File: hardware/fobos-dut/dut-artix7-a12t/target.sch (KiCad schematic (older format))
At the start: 34 parts, among them J1 Target, J2 Pmod 2x6, U2 SP3003-04ATG, U3 SP3003-04ATG, U4 SP3003-04ATG, U7 TS3A27518EIPWRQ1

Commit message: Schematic is 99% complete, getting started on layout
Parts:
- J2: footprint (none) -> Connector_PinHeader_2.54mm:PinHeader_2x06_P2.54mm_Horizontal
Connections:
- net labels added: +3V3
- net labels removed: VCCIO
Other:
- note added: "Make footprint compatible with Digilent inc PMOD standard"
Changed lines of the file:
@@
 $Descr USLetter 11000 8500
 encoding utf-8
-Sheet 2 6
+Sheet 2 7
 Title "FOBOS Artix-7 a12t DUT - Connectors, IO"
 Date "2020-07-28"
@@
 F 0 "J2" H 8250 6067 50  0000 C CNN
 F 1 "Pmod 2x6" H 8250 5976 50  0000 C CNN
-F 2 "" H 8200 5650 50  0001 C CNN
+F 2 "Connector_PinHeader_2.54mm:PinHeader_2x06_P2.54mm_Horizontal" H 8200 5650 50  0001 C CNN
 F 3 "~" H 8200 5650 50  0001 C CNN
 	1    8200 5650
@@
 	7850 5850 7850 6050
 Wire Wire Line
-	8250 6350 8250 6250
-Wire Wire Line
 	8250 6350 8550 6350
 Wire Wire Line
@@
 Wire Wire Line
 	4000 2500 4250 2500
-$Comp
-L cerg:VCCIO #PWR0111
-U 1 1 5F26D720
-P 8250 6250
-F 0 "#PWR0111" H 8250 6100 50  0001 C CNN
-F 1 "VCCIO" V 8150 6350 50  0000 C CNN
-F 2 "" H 8250 6250 50  0001 C CNN
-F 3 "" H 8250 6250 50  0001 C CNN
-	1    8250 6250
-	1    0    0    -1
-$EndComp
 Text GLabel 9900 3700 2    50   Input ~ 0
 (Aux)FC_PROG
@@
 	1    0    0    -1
 $EndComp
+Text Notes 7100 6500 0    50   ~ 0
+Make footprint compatible with Digilent inc PMOD standard
+$Comp
+L power:+3V3 #PWR?
+U 1 1 60336087
+P 8250 6300
+AR Path="/5F3A1954/60336087" Ref="#PWR?"  Part="1"
+AR Path="/5F20DA36/60336087" Ref="#PWR0111"  Part="1"
+F 0 "#PWR0111" H 8250 6150 50  0001 C CNN
+F 1 "+3V3" H 8265 6473 50  0000 C CNN
+F 2 "" H 8250 6300 50  0001 C CNN
+F 3 "" H 8250 6300 50  0001 C CNN
+	1    8250 6300
+	1    0    0    -1
+$EndComp
+Wire Wire Line
+	8250 6300 8250 6350
 $EndSCHEMATC

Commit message: Preliminary placement underway Made a copy of cerg 3d model within Artix 7 dut project to resolve nagging library path issue
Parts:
- removed U7: TS3A27518EIPWRQ1, Package_SO:TSSOP-24_4.4x7.8mm_P0.65mm, symbol cerg:TS3A27518EIPWRQ1
- added R67: 0R, Resistor_SMD:R_0603_1608Metric, symbol Device:R
- added U7: TS3A5018DBQR, cerg:SSOP-16_4.0x5.0mm_P0.635mm, symbol cerg:TS3A5018DBQR
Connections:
- wire segments 169 -> 167
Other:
- moved on the sheet: C54, R51
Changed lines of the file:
@@
 	1    0    0    1
 $EndComp
-Text GLabel 1550 5050 0    50   Input ~ 0
+Text GLabel 1750 5250 0    50   Input ~ 0
 FC_PROG
-Text GLabel 2700 5550 0    50   Input ~ 0
-FD_TF
-Text GLabel 2700 5350 0    50   Input ~ 0
-SW_DONE
 Text Notes 2200 4050 0    79   ~ 0
 Programming/DUT Communication Switches
@@
 L Device:R R?
 U 1 1 60131BF4
-P 1850 5250
+P 2050 5450
 AR Path="/5F227C5D/60131BF4" Ref="R?"  Part="1"
 AR Path="/5F20DA36/60131BF4" Ref="R51"  Part="1"
-F 0 "R51" V 1750 5200 50  0000 L CNN
-F 1 "10KR" V 1950 5150 50  0000 L CNN
-F 2 "Resistor_SMD:R_0603_1608Metric" V 1780 5250 50  0001 C CNN
-F 3 "~" H 1850 5250 50  0001 C CNN
-	1    1850 5250
+F 0 "R51" V 1950 5400 50  0000 L CNN
+F 1 "10KR" V 2150 5350 50  0000 L CNN
+F 2 "Resistor_SMD:R_0603_1608Metric" V 1980 5450 50  0001 C CNN
+F 3 "~" H 2050 5450 50  0001 C CNN
+	1    2050 5450
 	-1   0    0    1
 $EndComp
 Wire Wire Line
-	1850 5100 1850 5050
-$Comp
-L cerg:TS3A27518EIPWRQ1 U7
-U 1 1 601820C1
-P 3000 4950
-F 0 "U7" H 3650 5000 50  0000 C CNN
-F 1 "TS3A27518EIPWRQ1" H 4000 3400 50  0000 C CNN
-F 2 "Package_SO:TSSOP-24_4.4x7.8mm_P0.65mm" H 4000 5200 50  0001 C CNN
-F 3 "https://www.digikey.com/en/products/detail/texas-instruments/TS3A27518EIPWRQ1/2520836" H 4000 5200 50  0001 C CNN
-	1    3000 4950
-	1    0    0    -1
-$EndComp
-Text GLabel 2700 5850 0    50   Input ~ 0
-FC_DIO0_MUX
-Text GLabel 2700 5750 0    50   Input ~ 0
-SW_CLK
-Text GLabel 2700 5950 0    50   Input ~ 0
-FC_DIO0
-Text GLabel 2700 6300 0    50   Input ~ 0
-FC_DIO1
-Text GLabel 2700 6200 0    50   Input ~ 0
-FC_DIO1_MUX
-Text GLabel 2700 6100 0    50   Input ~ 0
-SW_DIN
-Text GLabel 4250 5550 2    50   Input ~ 0
-FC_DIO2
-Text GLabel 4250 5350 2    50   Input ~ 0
-SW_PROGRAM_B
-Text GLabel 4250 5450 2    50   Input ~ 0
-FC_DIO2_MUX
-Text GLabel 4250 5850 2    50   Input ~ 0
-FC_DIO3_MUX
-Text GLabel 4250 5750 2    50   Input ~ 0
-SW_INIT_B
-Text GLabel 4250 5950 2    50   Input ~ 0
-FC_DIO3
-Wire Wire Line
-	2700 5350 2900 5350
-Wire Wire Line
-	2700 5550 2900 5550
-Wire Wire Line
-	2700 5750 2900 5750
-Wire Wire Line
-	2700 5850 2900 5850
-Wire Wire Line
-	2700 5950 2900 5950
-Wire Wire Line
-	2700 6100 2900 6100
-Wire Wire Line
-	2700 6200 2900 6200
-Wire Wire Line
-	2700 6300 2900 6300
-Wire Wire Line
-	4250 5350 4050 5350
-Wire Wire Line
-	4250 5450 4050 5450
-Wire Wire Line
-	4250 5550 4050 5550
-Wire Wire Line
-	4250 5750 4050 5750
-Wire Wire Line
-	4250 5850 4050 5850
-Wire Wire Line
-	4250 5950 4050 5950
+	2050 5300 2050 5250
 $Comp
 L Device:C C?
 U 1 1 6025643D
-P 4350 4700
+P 4850 5500
 AR Path="/5F227C5D/6025643D" Ref="C?"  Part="1"
 AR Path="/5F20DA36/6025643D" Ref="C54"  Part="1"
-F 0 "C54" V 4200 4650 50  0000 L CNN
-F 1 "100nF" V 4500 4550 50  0000 L CNN
-F 2 "Capacitor_SMD:C_0603_1608Metric" H 4388 4550 50  0001 C CNN
-F 3 "~" H 4350 4700 50  0001 C CNN
-	1    4350 4700
-	1    0    0    -1
-$EndComp
-Text GLabel 4500 4450 2    50   Input ~ 0
+F 0 "C54" V 4700 5450 50  0000 L CNN
+F 1 "100nF" V 5000 5350 50  0000 L CNN
+F 2 "Capacitor_SMD:C_0603_1608Metric" H 4888 5350 50  0001 C CNN
+F 3 "~" H 4850 5500 50  0001 C CNN
+	1    4850 5500
+	1    0    0    -1
+$EndComp
+Text GLabel 5000 5250 2    50   Input ~ 0
 FC_3V3
 Wire Wire Line
-	3450 4850 3450 4450
-Wire Wire Line
-	3450 4450 4150 4450
-Wire Wire Line
-	4350 4550 4350 4450
-Connection ~ 4350 4450
-Wire Wire Line
-	4350 4450 4500 4450
-Wire Wire Line
-	4050 5050 4150 5050
-Wire Wire Line
-	4150 5050 4150 4450
-Connection ~ 4150 4450
-Wire Wire Line
-	4150 4450 4350 4450
+	4850 5350 4850 5250
+Connection ~ 4850 5250
+Wire Wire Line
+	4850 5250 5000 5250
 $Comp
 L power:GND #PWR?
 U 1 1 602946AE
-P 4350 4850
+P 4850 5650
 AR Path="/5B6C87CC/602946AE" Ref="#PWR?"  Part="1"
 AR Path="/5B5AB131/602946AE" Ref="#PWR?"  Part="1"
@@
 AR Path="/5F227C5D/602946AE" Ref="#PWR?"  Part="1"
 AR Path="/5F20DA36/602946AE" Ref="#PWR041"  Part="1"
-F 0 "#PWR041" H 4350 4600 50  0001 C CNN
-F 1 "GND" H 4355 4677 50  0000 C CNN
-F 2 "" H 4350 4850 50  0001 C CNN
-F 3 "" H 4350 4850 50  0001 C CNN
-	1    4350 4850
-	1    0    0    -1
-$EndComp
-Wire Wire Line
-	1550 5050 1850 5050
-Wire Wire Line
-	2900 5050 2800 5050
-Connection ~ 1850 5050
+F 0 "#PWR041" H 4850 5400 50  0001 C CNN
+F 1 "GND" H 4855 5477 50  0000 C CNN
+F 2 "" H 4850 5650 50  0001 C CNN
+F 3 "" H 4850 5650 50  0001 C CNN
+	1    4850 5650
+	1    0    0    -1
+$EndComp
+Wire Wire Line
+	1750 5250 2050 5250
 $Comp
 L power:GND #PWR?
 U 1 1 602A9678
-P 1850 5400
+P 2050 5600
 AR Path="/5B6C87CC/602A9678" Ref="#PWR?"  Part="1"
 AR Path="/5B5AB131/602A9678" Ref="#PWR?"  Part="1"
@@
 AR Path="/5F227C5D/602A9678" Ref="#PWR?"  Part="1"
 AR Path="/5F20DA36/602A9678" Ref="#PWR039"  Part="1"
-F 0 "#PWR039" H 1850 5150 50  0001 C CNN
-F 1 "GND" H 1855 5227 50  0000 C CNN
-F 2 "" H 1850 5400 50  0001 C CNN
-F 3 "" H 1850 5400 50  0001 C CNN
-	1    1850 5400
-	1    0    0    -1
-$EndComp
-Wire Wire Line
-	2900 5150 2800 5150
-Wire Wire Line
-	2800 5150 2800 5050
-Connection ~ 2800 5050
-Wire Wire Line
-	2800 5050 1850 5050
-$Comp
-L power:GND #PWR?
-U 1 1 602B3FF7
-P 3450 6500
-AR Path="/5B6C87CC/602B3FF7" Ref="#PWR?"  Part="1"
-AR Path="/5B5AB131/602B3FF7" Ref="#PWR?"  Part="1"
-AR Path="/5BE3725D/602B3FF7" Ref="#PWR?"  Part="1"
-AR Path="/5F227C5D/602B3FF7" Ref="#PWR?"  Part="1"
-AR Path="/5F20DA36/602B3FF7" Ref="#PWR040"  Part="1"
-F 0 "#PWR040" H 3450 6250 50  0001 C CNN
-F 1 "GND" H 3455 6327 50  0000 C CNN
-F 2 "" H 3450 6500 50  0001 C CNN
-F 3 "" H 3450 6500 50  0001 C CNN
-	1    3450 6500
+F 0 "#PWR039" H 2050 5350 50  0001 C CNN
+F 1 "GND" H 2055 5427 50  0000 C CNN
+F 2 "" H 2050 5600 50  0001 C CNN
+F 3 "" H 2050 5600 50  0001 C CNN
+	1    2050 5600
 	1    0    0    -1
 $EndComp
@@
 Wire Wire Line
 	8250 6300 8250 6350
+$Comp
+L cerg:TS3A5018DBQR U7
+U 1 1 602ABBA0
+P 3100 5150
+F 0 "U7" H 3425 5315 50  0000 C CNN
+F 1 "TS3A5018DBQR" H 3425 5224 50  0000 C CNN
+F 2 "cerg:SSOP-16_4.0x5.0mm_P0.635mm" H 3000 5400 50  0001 C CNN
+F 3 "https://www.digikey.com/en/products/detail/texas-instruments/TS3A5018DBQR/705733" H 3000 5400 50  0001 C CNN
+	1    3100 5150
+	1    0    0    -1
+$EndComp
+Text GLabel 2900 5450 0    50   Input ~ 0
+SW_CLK
+Text GLabel 2900 5350 0    50   Input ~ 0
+FC_DIO0_MUX
+Text GLabel 2900 5550 0    50   Input ~ 0
+FC_DIO0
+Text GLabel 2900 5750 0    50   Input ~ 0
+SW_DIN
+Text GLabel 2900 5650 0    50   Input ~ 0
+FC_DIO1_MUX
+Text GLabel 2900 5850 0    50   Input ~ 0
+FC_DIO1
+Text GLabel 4000 5950 2    50   Input ~ 0
+FC_DIO3
+Text GLabel 4000 5750 2    50   Input ~ 0
+FC_DIO3_MUX
+Text GLabel 4000 5850 2    50   Input ~ 0
+SW_INIT_B
+Text GLabel 4000 5650 2    50   Input ~ 0
+FC_DIO2
+Text GLabel 4000 5450 2    50   Input ~ 0
+FC_DIO2_MUX
+Text GLabel 4000 5550 2    50   Input ~ 0
+SW_PROGRAM_B
+Wire Wire Line
+	3000 5250 2050 5250
+Connection ~ 2050 5250
+Wire Wire Line
+	3000 5350 2900 5350
+Wire Wire Line
+	3000 5450 2900 5450
+Wire Wire Line
+	3000 5550 2900 5550
+Wire Wire Line
+	3000 5650 2900 5650
+Wire Wire Line
+	3000 5750 2900 5750
+Wire Wire Line
+	3000 5850 2900 5850
+Wire Wire Line
+	4000 5450 3850 5450
+Wire Wire Line
+	4000 5550 3850 5550
+Wire Wire Line
+	4000 5650 3850 5650
+Wire Wire Line
+	4000 5750 3850 5750
+Wire Wire Line
+	4000 5850 3850 5850
+Wire Wire Line
+	4000 5950 3850 5950
+Wire Wire Line
+	3850 5250 4000 5250
+Wire Wire Line
+	3850 5350 4000 5350
+Wire Wire Line
+	4000 5350 4000 5250
+Connection ~ 4000 5250
+Wire Wire Line
+	4000 5250 4850 5250
+Text GLabel 2650 6500 0    50   Input ~ 0
+SW_DONE
+Text GLabel 2650 6900 0    50   Input ~ 0
+FD_TF
+$Comp
+L Device:R R?
+U 1 1 603A6505
+P 2850 6700
+AR Path="/5F227C5D/603A6505" Ref="R?"  Part="1"
+AR Path="/5F20DA36/603A6505" Ref="R67"  Part="1"
+F 0 "R67" V 2750 6650 50  0000 L CNN
+F 1 "0R" V 2950 6600 50  0000 L CNN
+F 2 "Resistor_SMD:R_0603_1608Metric" V 2780 6700 50  0001 C CNN
+F 3 "~" H 2850 6700 50  0001 C CNN
+	1    2850 6700
+	-1   0    0    1
+$EndComp
+Wire Wire Line
+	2850 6550 2850 6500
+Wire Wire Line
+	2850 6500 2650 6500
+Wire Wire Line
+	2850 6850 2850 6900
+Wire Wire Line
+	2850 6900 2650 6900
 $EndSCHEMATC

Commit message: Coarse placement of all components within board outline, began to route traces
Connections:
- net labels removed: (Aux)FC_PROG, (Ready)FC2D_HS, (Valid)FD2C_HS
- wire segments 167 -> 169
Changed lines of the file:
@@
 	1    0    0    1
 $EndComp
-Text GLabel 9900 2150 2    50   Input ~ 0
+Text GLabel 8600 1950 0    50   Input ~ 0
 FC_DIO0
 Text GLabel 9900 1950 2    50   Input ~ 0
@@
 	9750 2150 9800 2150
 Wire Wire Line
-	8600 2150 8700 2150
-Text GLabel 8600 1950 0    50   Input ~ 0
+	8600 3700 8700 3700
+Text GLabel 9900 3700 2    50   Input ~ 0
 FC_IO
 Connection ~ 8700 1950
@@
 Wire Wire Line
 	8700 2350 8700 2150
-Connection ~ 8700 2150
 Wire Wire Line
 	8700 2150 8750 2150
@@
 Wire Wire Line
 	9250 2750 9250 2650
-Text GLabel 8600 3700 0    50   Input ~ 0
+Text GLabel 9900 3900 2    50   Input ~ 0
 FC2D_CLK
 Wire Wire Line
-	8600 3700 8700 3700
-Wire Wire Line
 	8600 3900 8700 3900
 Wire Wire Line
@@
 Wire Wire Line
 	8700 3500 8750 3500
-Connection ~ 8700 3700
 Wire Wire Line
 	8700 3700 8750 3700
@@
 Wire Wire Line
 	4000 2500 4250 2500
-Text GLabel 9900 3700 2    50   Input ~ 0
-(Aux)FC_PROG
-Text GLabel 9900 3900 2    50   Input ~ 0
+Text GLabel 7500 2150 2    50   Input ~ 0
+FC_PROG
+Text GLabel 8600 2150 0    50   Input ~ 0
 FD_TF
 Text GLabel 8600 3900 0    50   Input ~ 0
 FD2C_CLK
+Text GLabel 9900 2150 2    50   Input ~ 0
+FC2D_HS
 Text GLabel 6200 2150 0    50   Input ~ 0
-(Ready)FC2D_HS
-Text GLabel 7500 2150 2    50   Input ~ 0
-(Valid)FD2C_HS
+FD2C_HS
 Wire Wire Line
 	7200 1300 7250 1300
@@
 Wire Wire Line
 	6750 1300 6850 1300
-Text GLabel 8600 2150 0    50   Input ~ 0
+Text GLabel 8600 3700 0    50   Input ~ 0
 FC_RST
 Text Notes 7650 1100 0    79   ~ 0
@@
 Wire Wire Line
 	2850 6900 2650 6900
+Connection ~ 8700 3700
+Wire Wire Line
+	8600 2150 8700 2150
+Connection ~ 8700 2150
+$Comp
+L power:GND #PWR?
+U 1 1 60694C99
+P 2850 6100
+AR Path="/5F227C5D/60694C99" Ref="#PWR?"  Part="1"
+AR Path="/5F20DA36/60694C99" Ref="#PWR?"  Part="1"
+F 0 "#PWR?" H 2850 5850 50  0001 C CNN
+F 1 "GND" H 2855 5927 50  0000 C CNN
+F 2 "" H 2850 6100 50  0001 C CNN
+F 3 "" H 2850 6100 50  0001 C CNN
+	1    2850 6100
+	1    0    0    -1
+$EndComp
+Wire Wire Line
+	3000 5950 2850 5950
+Wire Wire Line
+	2850 5950 2850 6100
 $EndSCHEMATC

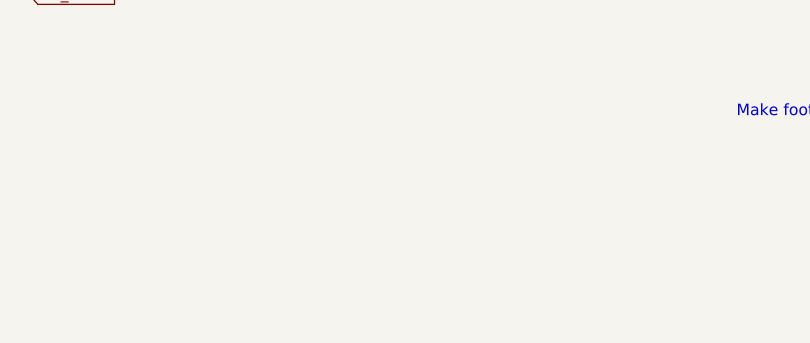
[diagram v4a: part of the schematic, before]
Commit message: Expanded copper pours on layer 3 Connected NC mux pins to the FPGA
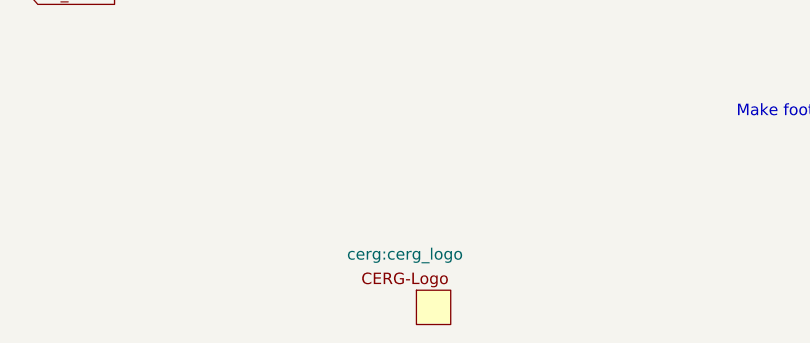
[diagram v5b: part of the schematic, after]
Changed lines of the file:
@@
 Wire Wire Line
 	2850 5950 2850 6100
+$Comp
+L cerg:CERG-logo #LOGO2
+U 1 1 606D810A
+P 5650 7250
+F 0 "#LOGO2" H 5650 7525 50  0001 C CNN
+F 1 "CERG-logo" H 5650 7025 50  0001 C CNN
+F 2 "cerg:cerg_logo" H 5650 7407 50  0000 C CNN
+F 3 "" H 5650 7525 50  0001 C CNN
+	1    5650 7250
+	1    0    0    -1
+$EndComp
 $EndSCHEMATC

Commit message: Added external 5V connector Added shunt for FC3v3 and 3V3 Added silkscreen which clarifies switch functionality Thickened 5 mil traces to 7 mil where feasible Moved Vcore amplifier closer to Vcore pad to reduce amplification of noise
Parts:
- added J10: Conn_01x02, Connector_Molex:Molex_KK-254_AE-6410-02A_1x02_P2.54mm_Vertical, symbol Connector_Generic:Conn_01x02
- added JP4: FC3V3_3V3_SHUNT, Connector_PinHeader_2.54mm:PinHeader_1x02_P2.54mm_Vertical, symbol Jumper:Jumper_2_Open
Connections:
- net labels added: +3.3V
- wire segments 169 -> 174
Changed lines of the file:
@@
 	1    0    0    1
 $EndComp
-Text GLabel 8600 1950 0    50   Input ~ 0
-FC_DIO0
-Text GLabel 9900 1950 2    50   Input ~ 0
-FC_DIO1
-Wire Wire Line
-	8600 1950 8700 1950
 Wire Wire Line
 	9750 1950 9800 1950
@@
 Text GLabel 9900 3700 2    50   Input ~ 0
 FC_IO
-Connection ~ 8700 1950
 Wire Wire Line
 	8700 1950 8750 1950
@@
 Text GLabel 7500 2150 2    50   Input ~ 0
 FC_PROG
-Text GLabel 8600 2150 0    50   Input ~ 0
-FD_TF
 Text GLabel 8600 3900 0    50   Input ~ 0
 FD2C_CLK
-Text GLabel 9900 2150 2    50   Input ~ 0
-FC2D_HS
 Text GLabel 6200 2150 0    50   Input ~ 0
 FD2C_HS
@@
 Text GLabel 1750 5250 0    50   Input ~ 0
 FC_PROG
-Text Notes 2200 4050 0    79   ~ 0
+Text Notes 2250 4900 0    79   ~ 0
 Programming/DUT Communication Switches
 $Comp
@@
 	2850 6900 2650 6900
 Connection ~ 8700 3700
-Wire Wire Line
-	8600 2150 8700 2150
-Connection ~ 8700 2150
 $Comp
 L power:GND #PWR?
@@
 	1    0    0    -1
 $EndComp
+Text GLabel 8600 1950 0    50   Input ~ 0
+FD_TF
+Wire Wire Line
+	8600 1950 8700 1950
+Text GLabel 8600 2150 0    50   Input ~ 0
+FC_DIO0
+Wire Wire Line
+	8600 2150 8700 2150
+Text GLabel 9900 2150 2    50   Input ~ 0
+FC_DIO1
+Text GLabel 9900 1950 2    50   Input ~ 0
+FC2D_HS
+$Comp
+L Connector_Generic:Conn_01x02 J?
+U 1 1 60A59B2F
+P 4300 2850
+AR Path="/5F449901/60A59B2F" Ref="J?"  Part="1"
+AR Path="/5F20DA36/60A59B2F" Ref="J10"  Part="1"
+F 0 "J10" H 4380 2842 50  0000 L CNN
+F 1 "Conn_01x02" H 4380 2751 50  0000 L CNN
+F 2 "Connector_Molex:Molex_KK-254_AE-6410-02A_1x02_P2.54mm_Vertical" H 4300 2850 50  0001 C CNN
+F 3 "~" H 4300 2850 50  0001 C CNN
+	1    4300 2850
+	1    0    0    -1
+$EndComp
+$Comp
+L Jumper:Jumper_2_Open JP?
+U 1 1 60A66495
+P 4200 3350
+AR Path="/5F449901/60A66495" Ref="JP?"  Part="1"
+AR Path="/5F20DA36/60A66495" Ref="JP4"  Part="1"
+F 0 "JP4" H 4200 3585 50  0000 C CNN
+F 1 "FC3V3_3V3_SHUNT" H 4200 3494 50  0000 C CNN
+F 2 "Connector_PinHeader_2.54mm:PinHeader_1x02_P2.54mm_Vertical" H 4200 3350 50  0001 C CNN
+F 3 "~" H 4200 3350 50  0001 C CNN
+	1    4200 3350
+	1    0    0    -1
+$EndComp
+Text GLabel 3800 3350 0    50   Input ~ 0
+FC_3V3
+Text GLabel 3800 2850 0    50   Input ~ 0
+FC_5V
+$Comp
+L power:GND #PWR?
+U 1 1 60A8FBF0
+P 3650 3000
+AR Path="/5B6C87CC/60A8FBF0" Ref="#PWR?"  Part="1"
+AR Path="/5B5AB131/60A8FBF0" Ref="#PWR?"  Part="1"
+AR Path="/5BE3725D/60A8FBF0" Ref="#PWR?"  Part="1"
+AR Path="/5F227C5D/60A8FBF0" Ref="#PWR?"  Part="1"
+AR Path="/5F20DA36/60A8FBF0" Ref="#PWR030"  Part="1"
+F 0 "#PWR030" H 3650 2750 50  0001 C CNN
+F 1 "GND" H 3655 2827 50  0000 C CNN
+F 2 "" H 3650 3000 50  0001 C CNN
+F 3 "" H 3650 3000 50  0001 C CNN
+	1    3650 3000
+	1    0    0    -1
+$EndComp
+Wire Wire Line
+	3800 2850 4100 2850
+Wire Wire Line
+	3650 3000 3650 2950
+Wire Wire Line
+	3650 2950 4100 2950
+Wire Wire Line
+	4000 3350 3800 3350
+$Comp
+L power:+3.3V #PWR?
+U 1 1 60ABDA54
+P 4700 3350
+AR Path="/5F449901/60ABDA54" Ref="#PWR?"  Part="1"
+AR Path="/5F20DA36/60ABDA54" Ref="#PWR031"  Part="1"
+F 0 "#PWR031" H 4700 3200 50  0001 C CNN
+F 1 "+3.3V" H 4715 3523 50  0000 C CNN
+F 2 "" H 4700 3350 50  0001 C CNN
+F 3 "" H 4700 3350 50  0001 C CNN
+	1    4700 3350
+	1    0    0    -1
+$EndComp
+Wire Wire Line
+	4700 3350 4400 3350
 $EndSCHEMATC

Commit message: Added Manufacturer Part Number, Manufacturer to all components except ferrite beads Added digikey quote
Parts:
- C1, C2, C3, C54: Description (none) -> CAP CER 0.1UF 6.3V X7R 0603; MPN (none) -> 06036C104KAT4A; Manufacturer (none) -> AVX Corporation
- J1: Description (none) -> CONN HEADER R/A 20POS 2.54MM; MPN (none) -> 61202021721; Manufacturer (none) -> Würth Elektronik
- J10: Description (none) -> CONN HEADER VERT 2POS 2.54MM; MPN (none) -> 0022272021; Manufacturer (none) -> Molex
- J2: Description (none) -> CONN HEADER R/A 12POS 2.54MM; MPN (none) -> PH2RA-12-UA; Manufacturer (none) -> Adam Tech
- JP4: Description (none) -> CONN HEADER VERT 2POS 2.54MM; MPN (none) -> 10129378-902001BLF; Manufacturer (none) -> Amphenol ICC (FCI)
- R1, R13, R14, R15, R16, R17, R18, R2, R3, R4, R5, R6: Description (none) -> RES 22 OHM 5% 1/10W 0603 SMD; MPN (none) -> ERJ-U03J220V; Manufacturer (none) -> Panasonic Electronic Components
- R10, R11, R12, R19, R20, R7, R8, R9: Description (none) -> RES SMD 200 OHM 0.5% 1/10W 0603; MPN (none) -> ERA-3AED201V; Manufacturer (none) -> Panasonic Electronic Components
- R51: Description (none) -> RES SMD 10K OHM 1% 1/10W 0603; MPN (none) -> ERJ-3EKF1002V; Manufacturer (none) -> Panasonic Electronic Components
- R67: Description (none) -> RES 0 OHM JUMPER 1/10W 0603; MPN (none) -> RMCF0603ZT0R00; Manufacturer (none) -> Stackpole Electronics Inc
- TP2, TP3, TP4: Description (none) -> TEST POINT (BLACK) - MULTIPURPOS; MPN (none) -> 5281; Manufacturer (none) -> Keystone Electronics
- U2, U3, U4: Description (none) -> TVS DIODE 6V 15V 10MSOP; MPN (none) -> SP3003-04ATG; Manufacturer (none) -> Littelfuse Inc.
- U7: Description (none) -> IC SWITCH QUAD SPDT 16SSOP; MPN (none) -> TS3A5018DBQR; Manufacturer (none) -> Texas Instruments
